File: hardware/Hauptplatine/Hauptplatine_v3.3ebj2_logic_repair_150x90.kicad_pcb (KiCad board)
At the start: 2 copper layers, 150 x 90 mm, 30 parts, among them J1 230V IN L/N/PE, J2 REED OFFEN, J3 REED GEKIPPT, J4 RS485 5V/GND/A/B, J5 MOTOR N/PE/AUF/AB, J6 28BYJ-48 OBEN, J7 28BYJ-48 UNTEN, K1 Finder 40.52.9.005.0000 AUF, K2 Finder 40.52.9.005.0000 AB, Q1 BC337 AUF, Q2 BC337 AB, U1 ESP32-S3 DevKitC-1 headers, U2 AMS1117-3.3, U3 MAX3485, U4 ULN2003A OBEN, U5 ULN2003A UNTEN

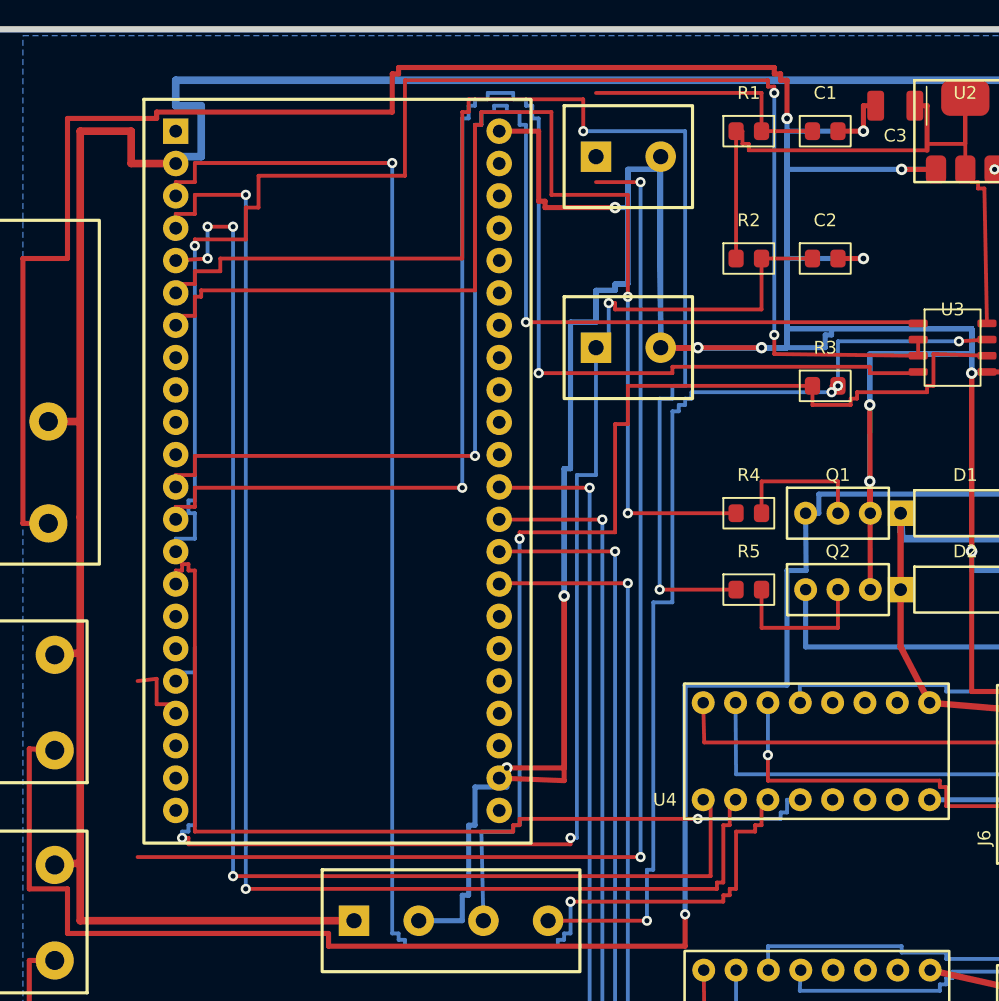
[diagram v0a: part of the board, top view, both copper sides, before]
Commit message: PCB v3.3ebj2: correct ESP32-S3 DevKitC-1 J1 power and GPIO assignments
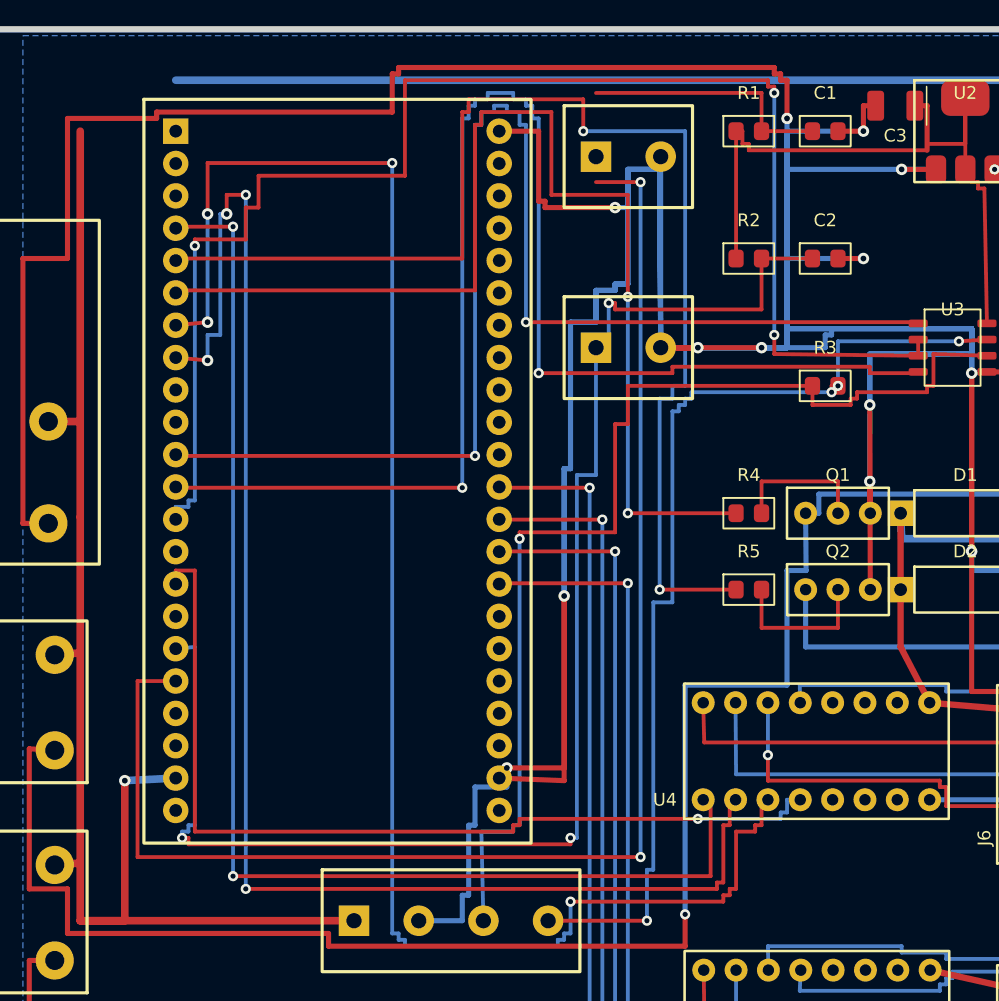
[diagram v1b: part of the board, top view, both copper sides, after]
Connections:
- U1 pad 1: /GND -> (no net)
- U1 pad 11: /ROLL_DN -> /ROLL_UP
- U1 pad 13: /ROLL_UP -> /STEP_TOP_3
- U1 pad 15: unconnected-(U1-Pin_15-Pad15) -> /STEP_TOP_2
- U1 pad 21: unconnected-(U1-Pin_21-Pad21) -> /RS485_RX
- U1 pad 23: /RS485_RX -> /RS485_TX
- U1 pad 25: /RS485_TX -> /RS485_DE
- U1 pad 27: /RS485_DE -> (no net)
- U1 pad 3: /+5V -> (no net)
- U1 pad 33: unconnected-(U1-Pin_33-Pad33) -> /REED_TILT
- U1 pad 35: /REED_TILT -> /REED_OPEN
- U1 pad 37: /REED_OPEN -> unconnected-(U1-Pin_37-Pad37)
- U1 pad 41: unconnected-(U1-Pin_41-Pad41) -> /+5V
- U1 pad 5: /STEP_TOP_3 -> (no net)
- U1 pad 7: /STEP_TOP_2 -> /STEP_TOP_1
- U1 pad 9: /STEP_TOP_1 -> /ROLL_DN
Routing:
- net /REED_OPEN: track 121.7 -> 132.8 mm
- net /STEP_TOP_2: track 108.2 -> 118.5 mm, vias 2 -> 4
- net /STEP_TOP_3: track 122.1 -> 132.0 mm, vias 2 -> 4
- net /RS485_DE: track 119.1 -> 115.6 mm
- net /REED_TILT: track 117.2 -> 114.5 mm
- net /ROLL_UP: track 92.2 -> 89.7 mm
- net /ROLL_DN: track 101.7 -> 99.2 mm
- net /RS485_TX: track 115.2 -> 112.8 mm
- net /STEP_TOP_1: track 102.1 -> 99.7 mm, vias 4 -> 2
- net /RS485_RX: track 105.4 -> 103.3 mm
- net /+5V: track 302.7 -> 300.6 mm, vias 1 -> 2
- net /STEP_TOP_4: track 74.1 -> 73.1 mm
